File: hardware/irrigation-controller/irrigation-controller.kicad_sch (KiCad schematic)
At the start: 83 parts, among them J1 RS485, J10 I2C, J11 IO, J12 RELAY_2, J15 FLOW_1, J2 I2C, J3 ICSP, J4 UART, J5 RF Module, J6 PWR 24V, J7 RELAY_1, J8 RELAY_3, J9 RELAY_4, K1 RELAY_3, K2 RELAY_4, Q1 MMBT3904, Q2 MMBT3904, Q3 2N7002, Q4 2N7002, Q5 2N7002, Q6 2N7002, SW1 RESET, SW2 BUTTON, U1 AQY280EH, U2 ATmega328P-AU, U3 AQY280EH, U4 TPS54331DR, U5 TPS54331DR, U6 MAX485, Y1 8MHz

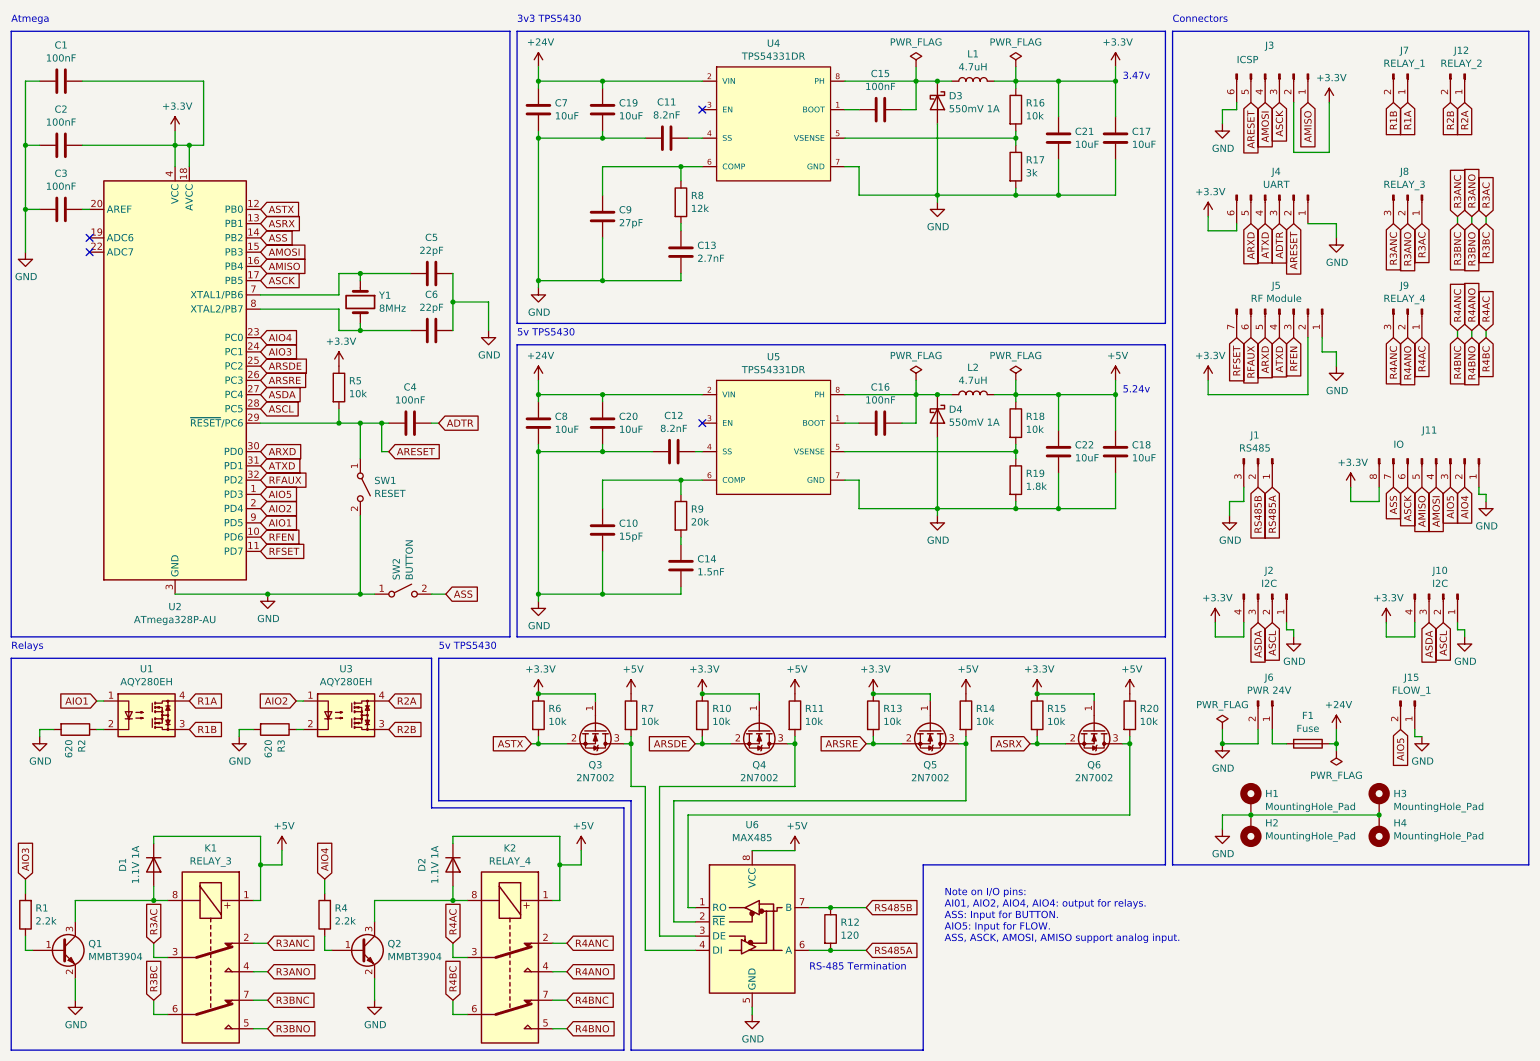
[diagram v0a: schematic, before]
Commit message: Update irrigation controller board
Remove atmega328p
Remove 5v voltage regulator
Replace max485 with max3485
Remove signal relays
Add female headers for ESP32
Add two LEDs
Update BOM based on JLCPCB availability
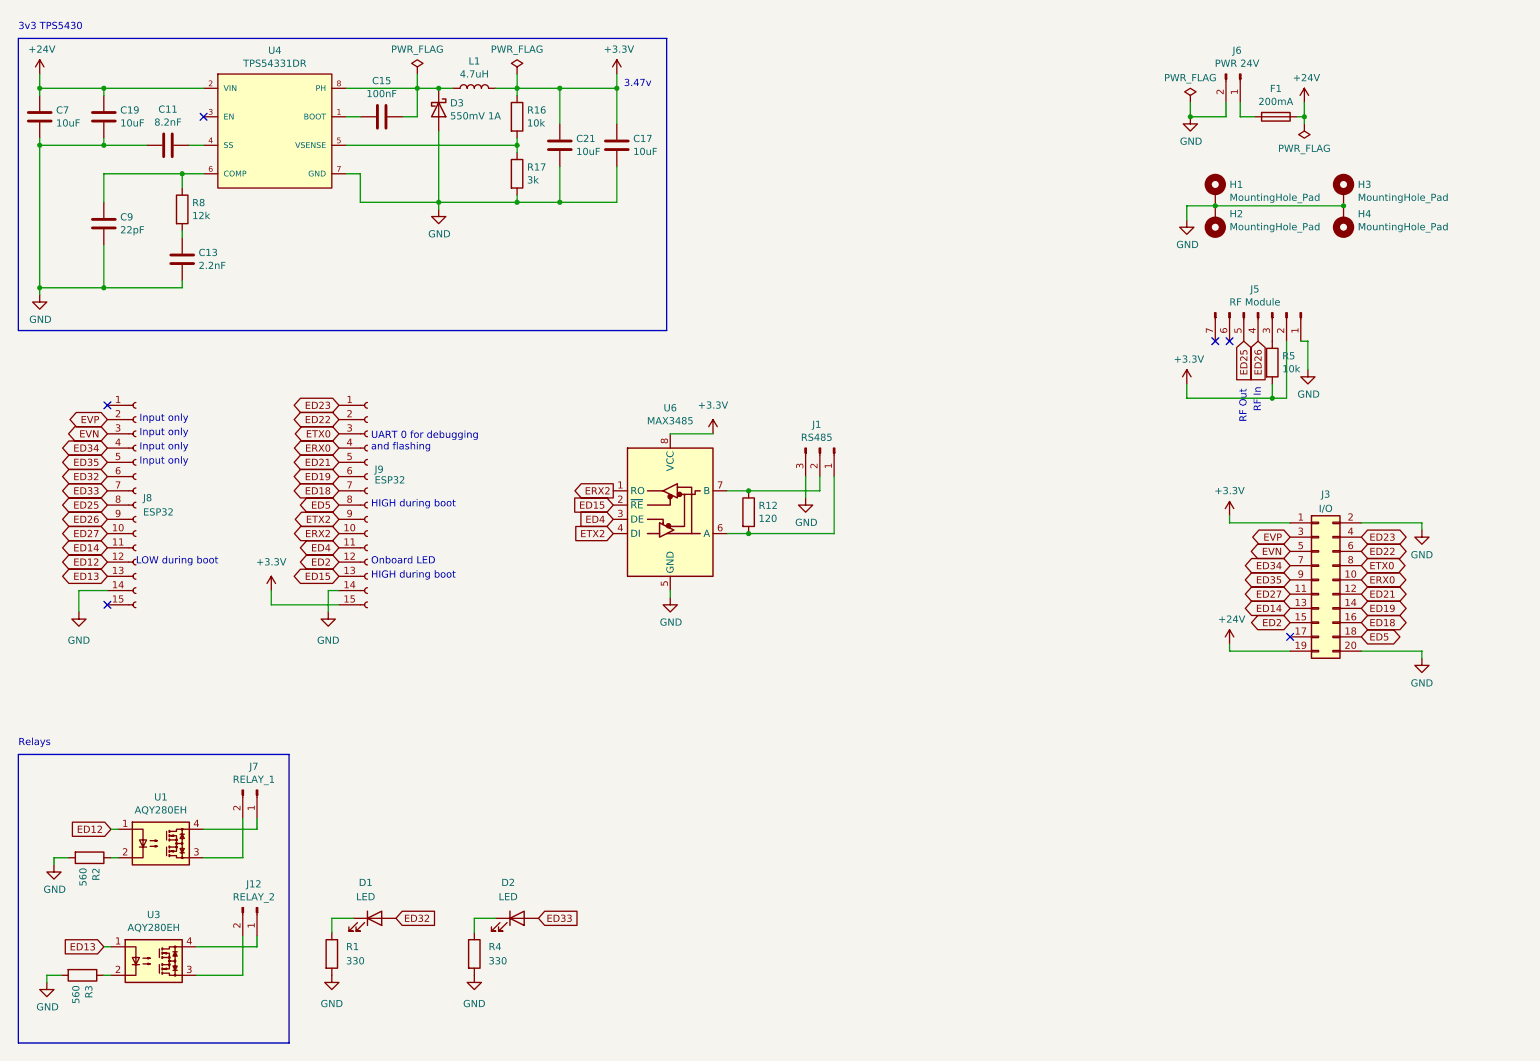
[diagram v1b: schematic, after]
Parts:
- removed C1, C16, C2, C3, C4: 100nF, Capacitor_SMD:C_0603_1608Metric, symbol Device:C
- removed C10: 15pF, Capacitor_SMD:C_0603_1608Metric, symbol Device:C
- removed C12: 8.2nF, Capacitor_SMD:C_0603_1608Metric, symbol Device:C
- removed C14: 1.5nF, Capacitor_SMD:C_0402_1005Metric, symbol Device:C
- removed C18, C20, C22, C8: 10uF, Capacitor_SMD:C_1206_3216Metric, symbol Device:C
- removed C5, C6: 22pF, Capacitor_SMD:C_0402_1005Metric, symbol Device:C
- removed D1, D2: 1.1V 1A, Diode_SMD:D_SMA, symbol Device:D
- removed D4: 550mV 1A, Diode_SMD:D_SMA, symbol Device:D_Schottky
- removed J10, J2: I2C, Connector_JST:JST_XH_B4B-XH-A_1x04_P2.50mm_Vertical, symbol Connector:Conn_01x04_Pin
- removed J11: IO, Connector_PinHeader_2.54mm:PinHeader_2x04_P2.54mm_Vertical, symbol Connector:Conn_01x08_Pin
- removed J15: FLOW_1, Connector_JST:JST_XH_B2B-XH-A_1x02_P2.50mm_Vertical, symbol Connector:Conn_01x02_Pin
- removed J3: ICSP, Connector_PinHeader_2.54mm:PinHeader_2x03_P2.54mm_Vertical, symbol Connector:Conn_01x06_Pin
- removed J4: UART, Connector_PinHeader_2.54mm:PinHeader_2x03_P2.54mm_Vertical, symbol Connector:Conn_01x06_Pin
- removed J8: RELAY_3, Connector_JST:JST_XH_B3B-XH-A_1x03_P2.50mm_Vertical, symbol Connector:Conn_01x03_Pin
- removed J9: RELAY_4, Connector_JST:JST_XH_B3B-XH-A_1x03_P2.50mm_Vertical, symbol Connector:Conn_01x03_Pin
- removed K1: RELAY_3, lib:Relay_DPDT_NEXEM_UA2_Pitch3.2mm, symbol lib:UA2-5NU
- removed K2: RELAY_4, lib:Relay_DPDT_NEXEM_UA2_Pitch3.2mm, symbol lib:UA2-5NU
- removed L2: 4.7uH, Capacitor_THT:C_Radial_D5.0mm_H5.0mm_P2.00mm, symbol Device:L
- removed Q1, Q2: MMBT3904, Package_TO_SOT_SMD:SOT-23, symbol Transistor_BJT:MMBT3904
- removed Q3, Q4, Q5, Q6: 2N7002, Package_TO_SOT_SMD:SOT-23, symbol Transistor_FET:2N7002
- removed R10, R11, R13, R14, R15, R18, R20, R6, R7: 10k, Resistor_SMD:R_0402_1005Metric, symbol Device:R
- removed R19: 1.8k, Resistor_SMD:R_0603_1608Metric, symbol Device:R
- removed R9: 20k, Resistor_SMD:R_0603_1608Metric, symbol Device:R
- removed SW1: RESET, lib:SW_SPST_THT_5.0mm, symbol Switch:SW_SPST
- removed SW2: BUTTON, lib:SW_SPST_THT_5.0mm, symbol Switch:SW_SPST
- removed U2: ATmega328P-AU, Package_QFP:TQFP-32_7x7mm_P0.8mm, symbol irrigation-controller-rescue:ATmega328P-AU-MCU_Microchip_ATmega
- removed U5: TPS54331DR, TPS54331DR:Texas_Instruments-TPS54331DR-Level_A, symbol irrigation-controller-rescue:TPS54331DR-TPS54331DR
- removed Y1: 8MHz, Crystal:Crystal_SMD_5032-2Pin_5.0x3.2mm, symbol Device:Crystal
- added D1, D2: LED, LED_SMD:LED_0603_1608Metric, symbol Device:LED
- added J3: I/O, Connector_PinHeader_2.54mm:PinHeader_2x10_P2.54mm_Vertical, symbol Connector_Generic:Conn_02x10_Odd_Even
- added J8, J9: ESP32, Connector_PinSocket_2.54mm:PinSocket_1x15_P2.54mm_Vertical, symbol Connector:Conn_01x15_Socket
- C11: JLCPCB Part C27920 -> C1322360
- C13: value 2.7nF -> 2.2nF; JLCPCB Part C1609 -> C1604
- C15, R16, R5: JLCPCB UP 0.01 -> (none)
- C17, C19, C21, C7: JLCPCB UP 0.07 -> (none)
- C9: value 27pF -> 22pF; JLCPCB Part C1656 -> C1653
- D3: JLCPCB UP 0.05 -> (none)
- F1: value Fuse -> 200mA
- J5: footprint Connector_PinSocket_2.54mm:PinSocket_1x07_P2.54mm_Vertical -> lib:YL_800T
- L1: footprint Capacitor_THT:C_Radial_D5.0mm_H5.0mm_P2.00mm -> Inductor_SMD:L_Changjiang_FNR4020S; JLCPCB Part (none) -> C167828; Purchase Link https://au.mouser.com/ProductDetail/Murata-Power-Solutions/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 -> NA (Extended)
- R1, R4: value 2.2k -> 330; JLCPCB Part C25879 -> C25104; JLCPCB UP 0.01 -> (none)
- R2, R3: value 620 -> 560; JLCPCB Part C23220 -> C23204; JLCPCB UP 0.01 -> (none)
- U4: Purchase Link NA -> NA (Extended)
- U6: value MAX485 -> MAX3485; symbol Interface_UART:MAX485E -> Interface_UART:MAX3485; Purchase Link https://au.element14.com/maxim-integrated-products/max485cp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 -> (none)
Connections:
- net +5V is gone; now on net +3.3V: U6.8 (VCC)
- net AIO3 is gone; now on net GND: R1.2
- net AIO4 is gone; now on net GND: R4.2
- net ARESET is gone; now on net +3.3V: R5.2
- net +24V: now also J3.19 (Pin_19)
- net +3.3V: now also J3.1 (Pin_1), J9.15 (Pin_15); no longer R5.1
- net GND: now also J3.2 (Pin_2), J3.20 (Pin_20), J8.14 (Pin_14), J9.14 (Pin_14)
- net at R1.1: now also D1.1 (K)
- net at R4.1: now also D2.1 (K)
- net ERX2: now reaches U6.1 (RO)
- net ERX2: now also J9.10 (Pin_10)
- net ED15: now reaches U6.2 (~{RE})
- net ED15: now also J9.13 (Pin_13)
- net ED4: now reaches U6.3 (DE)
- net ED4: now also J9.11 (Pin_11)
- net ETX2: now reaches U6.4 (DI)
- net ETX2: now also J9.9 (Pin_9)
- net AIO1 renamed ED12
- net ED12: now also J8.12 (Pin_12)
- net AIO2 renamed ED13
- net ED13: now also J8.13 (Pin_13)
- net ARXD renamed ED25
- net ED25: now also J8.8 (Pin_8)
- net ATXD renamed ED26
- net ED26: now also J8.9 (Pin_9)
- net R1A: no longer names the net of J7.1 (Pin_1), U1.4
- net R1B: no longer names the net of J7.2 (Pin_2), U1.3
- net R2A: no longer names the net of J12.1 (Pin_1), U3.4
- net R2B: no longer names the net of J12.2 (Pin_2), U3.3
- net RFAUX: no longer names the net of J5.6 (Pin_6)
- net RFEN: no longer names the net of J5.3 (Pin_3)
- net RFEN: now also R5.1
- net RFSET: no longer names the net of J5.7 (Pin_7)
- net RS485A: no longer names the net of J1.1 (Pin_1), R12.2, U6.6 (A)
- net RS485B: no longer names the net of J1.2 (Pin_2), R12.1, U6.7 (B)
- new net ED14: J3.13 (Pin_13), J8.11 (Pin_11)
- new net ED18: J3.16 (Pin_16), J9.7 (Pin_7)
- new net ED19: J3.14 (Pin_14), J9.6 (Pin_6)
- new net ED2: J3.15 (Pin_15), J9.12 (Pin_12)
- new net ED21: J3.12 (Pin_12), J9.5 (Pin_5)
- new net ED22: J3.6 (Pin_6), J9.2 (Pin_2)
- new net ED23: J3.4 (Pin_4), J9.1 (Pin_1)
- new net ED27: J3.11 (Pin_11), J8.10 (Pin_10)
- new net ED32: D1.2 (A), J8.6 (Pin_6)
- new net ED33: D2.2 (A), J8.7 (Pin_7)
- new net ED34: J3.7 (Pin_7), J8.4 (Pin_4)
- new net ED35: J3.9 (Pin_9), J8.5 (Pin_5)
- new net ED5: J3.18 (Pin_18), J9.8 (Pin_8)
- new net ERX0: J3.10 (Pin_10), J9.4 (Pin_4)
- new net ETX0: J3.8 (Pin_8), J9.3 (Pin_3)
- new net EVN: J3.5 (Pin_5), J8.3 (Pin_3)
- new net EVP: J3.3 (Pin_3), J8.2 (Pin_2)
- no-connect marks 4 -> 6
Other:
- note added: "HIGH during boot"
- note added: "Input only"
- note added: "LOW during boot"
- note added: "Onboard LED"
- note added: "RF In"
- note added: "RF Out"
- note added: "UART 0 for debugging and flashing"
- note removed: "5.24v"
- note removed: "5v TPS5430"
- note removed: "Atmega"
- note removed: "Connectors"
- note removed: "Note on I/O pins: AI01, AIO2, AIO4, AIO4: output for relays. ASS: Input for BUTTON. AIO5: Input for FLOW. ASS, ASCK, AMOSI, AMISO support analog input."
- note removed: "RS-485 Termination"
- moved on the sheet: C11, C13, C15, C17, C19, C21, C7, C9, D3, F1, H1, H2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

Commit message: Fix for controller RF EN pin
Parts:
- R5: value 10k -> 3k; footprint Resistor_SMD:R_0402_1005Metric -> Resistor_SMD:R_0603_1608Metric; JLCPCB Part C25744 -> C4211
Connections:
- net +3.3V: no longer R5.2
- net GND: now also R5.2
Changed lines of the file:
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@@
   (junction (at 88.9 25.4) (diameter 0) (color 0 0 0 0)
   )
-  (junction (at 237.49 80.645) (diameter 0) (color 0 0 0 0)
-  )
   (junction (at 29.21 35.56) (diameter 0) (color 0 0 0 0)
   )
@@
   )
   (junction (at 227.33 46.355) (diameter 0) (color 0 0 0 0)
+  )
+  (junction (at 242.57 79.375) (diameter 0) (color 0 0 0 0)
   )
   (junction (at 102.87 45.72) (diameter 0) (color 0 0 0 0)
@@
     (stroke (width 0) (type default))
   )
-  (wire (pts (xy 243.84 70.485) (xy 243.84 75.565))
+  (wire (pts (xy 242.57 79.375) (xy 242.57 81.915))
+    (stroke (width 0) (type default))
+  )
+  (wire (pts (xy 242.57 70.485) (xy 242.57 79.375))
     (stroke (width 0) (type default))
   )
@@
     (stroke (width 0) (type default))
   )
-  (wire (pts (xy 237.49 80.645) (xy 222.25 80.645))
-    (stroke (width 0) (type default))
-  )
   (wire (pts (xy 17.78 34.29) (xy 17.78 35.56))
     (stroke (width 0) (type default))
@@
     (stroke (width 0) (type default))
   )
+  (wire (pts (xy 237.49 78.105) (xy 237.49 79.375))
+    (stroke (width 0) (type default))
+  )
   (wire (pts (xy 240.665 102.87) (xy 229.87 102.87))
     (stroke (width 0) (type default))
@@
     (stroke (width 0) (type default))
   )
+  (wire (pts (xy 237.49 79.375) (xy 242.57 79.375))
+    (stroke (width 0) (type default))
+  )
   (wire (pts (xy 102.87 44.45) (xy 102.87 45.72))
     (stroke (width 0) (type default))
@@
     (stroke (width 0) (type default))
   )
-  (wire (pts (xy 237.49 78.105) (xy 237.49 80.645))
-    (stroke (width 0) (type default))
-  )
   (wire (pts (xy 59.055 117.475) (xy 71.12 117.475))
     (stroke (width 0) (type default))
@@
     (stroke (width 0) (type default))
   )
-  (wire (pts (xy 243.84 70.485) (xy 242.57 70.485))
-    (stroke (width 0) (type default))
-  )
   (wire (pts (xy 72.39 40.64) (xy 74.93 40.64))
     (stroke (width 0) (type default))
@@
     (stroke (width 0) (type default))
   )
-  (wire (pts (xy 240.03 80.645) (xy 237.49 80.645))
+  (wire (pts (xy 222.25 80.645) (xy 240.03 80.645))
     (stroke (width 0) (type default))
   )
@@
     )
   )
-  (symbol (lib_id "power:GND") (at 243.84 75.565 0) (unit 1)
-    (in_bom yes) (on_board yes) (dnp no)
-    (property "Reference" "#PWR039" (at 243.84 81.915 0)
-      (effects (font (size 1.27 1.27)) hide)
-    )
-    (property "Value" "GND" (at 243.967 79.9592 0)
-      (effects (font (size 1.27 1.27)))
-    )
-    (property "Footprint" "" (at 243.84 75.565 0)
-      (effects (font (size 1.27 1.27)) hide)
-    )
-    (property "Datasheet" "" (at 243.84 75.565 0)
+  (symbol (lib_id "power:GND") (at 242.57 81.915 0) (unit 1)
+    (in_bom yes) (on_board yes) (dnp no)
+    (property "Reference" "#PWR039" (at 242.57 88.265 0)
+      (effects (font (size 1.27 1.27)) hide)
+    )
+    (property "Value" "GND" (at 242.697 86.3092 0)
+      (effects (font (size 1.27 1.27)))
+    )
+    (property "Footprint" "" (at 242.57 81.915 0)
+      (effects (font (size 1.27 1.27)) hide)
+    )
+    (property "Datasheet" "" (at 242.57 81.915 0)
       (effects (font (size 1.27 1.27)) hide)
     )
@@
         (path "/eb6d9c11-1322-497a-b8f1-7adb02bbc7ab"
           (reference "#PWR014") (unit 1)
-        )
-      )
-    )
-  )
-  (symbol (lib_id "Device:R") (at 237.49 74.295 0) (unit 1)
-    (in_bom yes) (on_board yes) (dnp no)
-    (property "Reference" "R5" (at 239.268 73.1266 0)
-      (effects (font (size 1.27 1.27)) (justify left))
-    )
-    (property "Value" "10k" (at 239.268 75.438 0)
-      (effects (font (size 1.27 1.27)) (justify left))
-    )
-    (property "Footprint" "Resistor_SMD:R_0402_1005Metric" (at 235.712 74.295 90)
-      (effects (font (size 1.27 1.27)) hide)
-    )
-    (property "Datasheet" "" (at 237.49 74.295 0)
-      (effects (font (size 1.27 1.27)) hide)
-    )
-    (property "JLCPCB Part" "C25744" (at 237.49 74.295 0)
-      (effects (font (size 1.27 1.27)) hide)
-    )
-    (property "JLCPCB UP" "" (at 237.49 74.295 0)
-      (effects (font (size 1.27 1.27)) hide)
-    )
-    (property "JLCPCB Basic" "" (at 237.49 74.295 0)
-      (effects (font (size 1.27 1.27)) hide)
-    )
-    (property "Purchase Link" "NA" (at 237.49 74.295 0)
-      (effects (font (size 1.27 1.27)) hide)
-    )
-    (pin "1")
-    (pin "2")
-    (instances
-      (project "irrigation-controller"
-        (path "/eb6d9c11-1322-497a-b8f1-7adb02bbc7ab"
-          (reference "R5") (unit 1)
         )
       )
@@
         )
       )
+    )
+  )
+  (symbol (lib_id "Device:R") (at 237.49 74.295 0) (unit 1)
+    (in_bom yes) (on_board yes) (dnp no)
+    (property "Reference" "R5" (at 239.268 73.1266 0)
+      (effects (font (size 1.27 1.27)) (justify left))
+    )
+    (property "Value" "3k" (at 239.268 75.438 0)
+      (effects (font (size 1.27 1.27)) (justify left))
+    )
+    (property "Footprint" "Resistor_SMD:R_0603_1608Metric" (at 235.712 74.295 90)
+      (effects (font (size 1.27 1.27)) hide)
+    )
+    (property "Datasheet" "" (at 237.49 74.295 0)
+      (effects (font (size 1.27 1.27)) hide)
+    )
+    (property "JLCPCB Part" "C4211" (at 237.49 74.295 0)
+      (effects (font (size 1.27 1.27)) hide)
+    )
+    (property "Purchase Link" "NA" (at 237.49 74.295 0)
+      (effects (font (size 1.27 1.27)) hide)
+    )
+    (pin "1")
+    (pin "2")
+    (instances
+      (project "irrigation-controller"
+        (path "/eb6d9c11-1322-497a-b8f1-7adb02bbc7ab"
+          (reference "R5") (unit 1)
+        )
+      )
